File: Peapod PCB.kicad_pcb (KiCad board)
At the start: 2 copper layers, 16 parts, among them J1 CONN_01X01, J2 CONN_01X02, J3 CONN_01X06, J5 CONN_01X01, J6 CONN_01X01, J7 CONN_01X02, U1 ESP8266

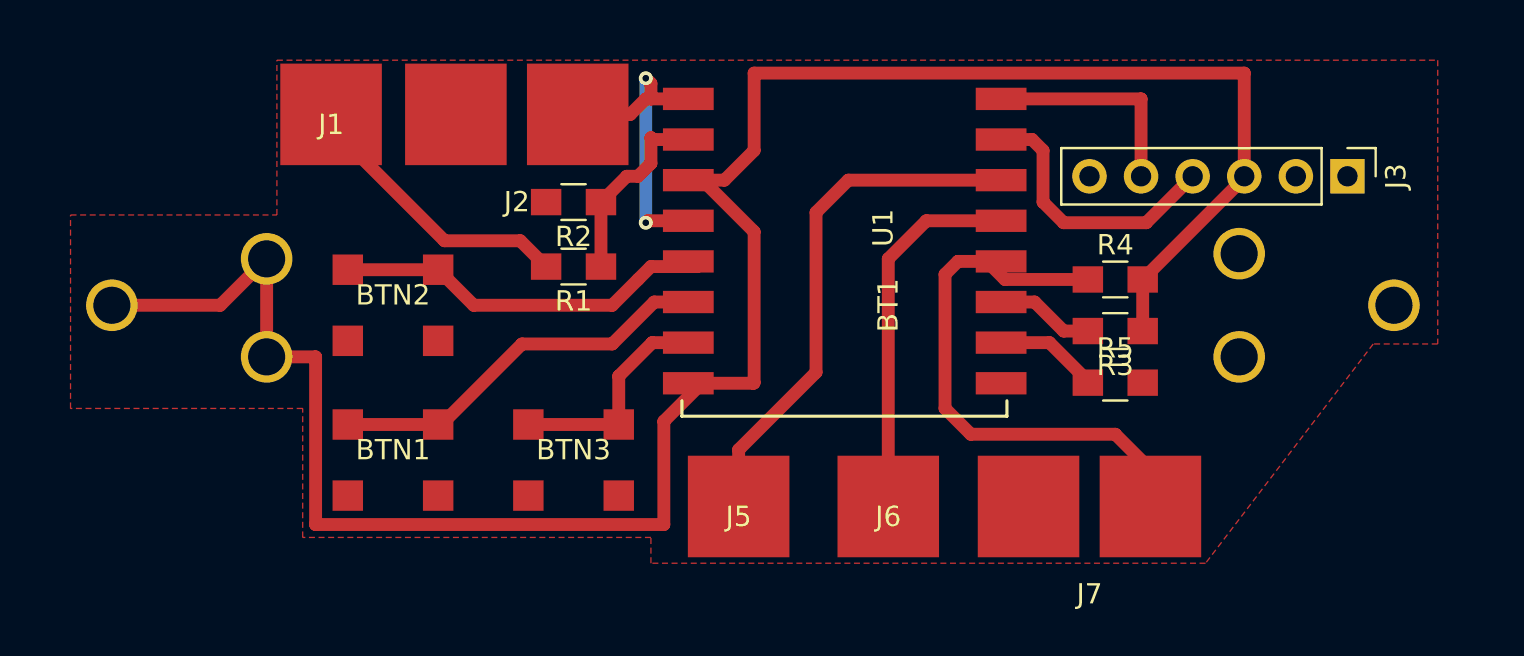
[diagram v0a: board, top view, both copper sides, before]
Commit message: changed copper to back plate
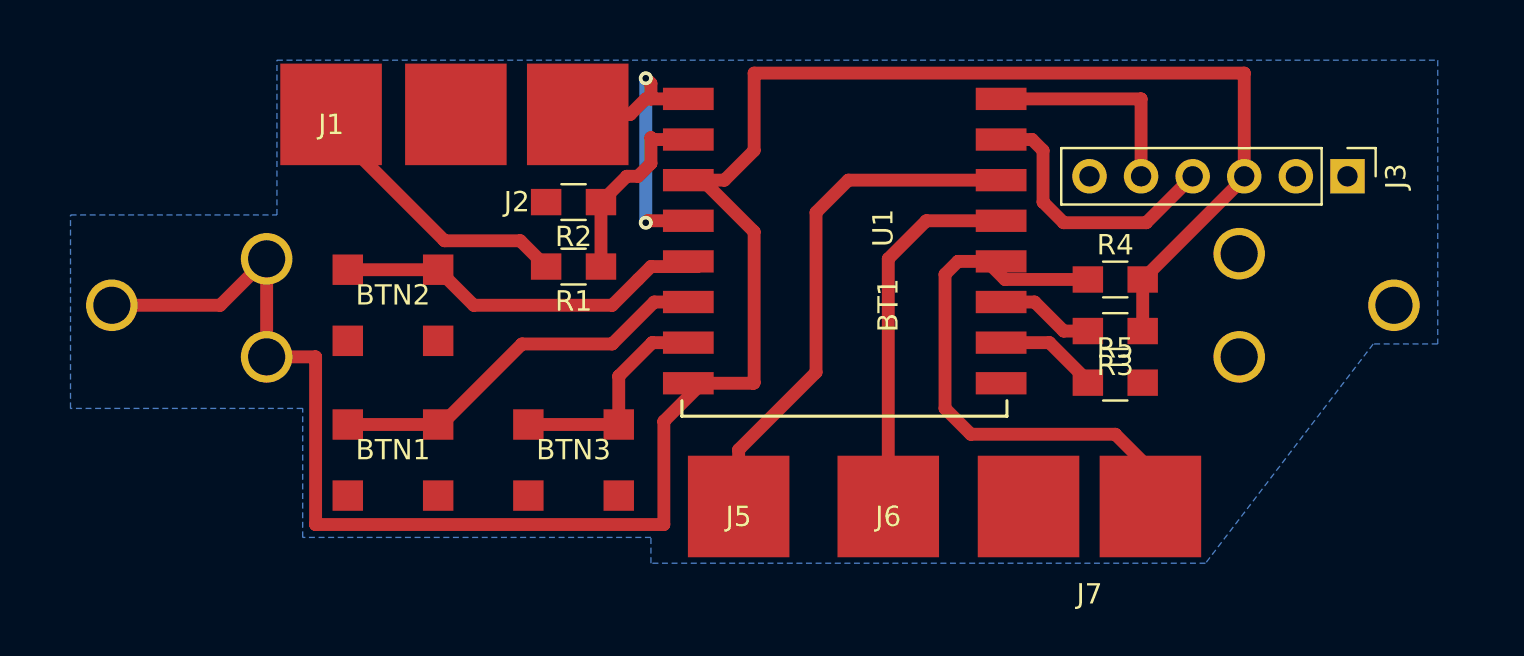
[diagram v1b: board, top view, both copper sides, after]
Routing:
- added copper zone on B.Cu, net GND
- removed copper zone on F.Cu, net GND
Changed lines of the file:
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@@
   (general
     (links 40)
-    (no_connects 4)
+    (no_connects 11)
     (area 154.305 20.282599 221.615001 54.6134)
     (thickness 1.6002)
@@
   (segment (start 204.39 43.1) (end 202.5 41.21) (width 0.635) (layer F.Cu) (net 17))
   (segment (start 202.5 41.21) (end 199.42 41.21) (width 0.635) (layer F.Cu) (net 17))
-  (zone (net 2) (net_name GND) (layer F.Cu) (hatch edge 0.508)
+  (zone (net 2) (net_name GND) (layer B.Cu) (hatch edge 0.508)
     (connect_pads (clearance 0.508))
     (min_thickness 0.254)

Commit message: stufff
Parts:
- added G***: LOGO, mod:LOGO, F.Cu at (159.5, 32.5)
- added J4: CONN_01X01, mod:Alligator Pad, F.Cu at (219.5, 49.3)
- added J8: CONN_01X01, mod:Alligator Pad, F.Cu at (213.4, 49.3)
- moved BTN2 12.7 mm to (160.0, 47.0)
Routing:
- net Net-(J3-Pad5): track 11.4 -> 47.3 mm, vias 0 -> 2
- net Net-(J3-Pad4): track 14.3 -> 30.8 mm, vias 0 -> 2
- net Net-(BTN2-Pad2): track 19.1 -> 32.4 mm
- net +3V3: track 108.4 -> 120.9 mm
- net GND: track 0.00 -> 0.20 mm, vias 0 -> 11
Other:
- board text added: "FSOSS 2017"

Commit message: Added labels
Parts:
- BRDG 2 RESET: renamed from J2
- VOTE :(: renamed from BTN3
- VOTE :): renamed from BTN2
- VOTE :|: renamed from BTN1
- moved ANALOG 1.27 mm to (165.9, 30.0)
- moved G*** 1.14 mm to (158.5, 33.0)
- renumbered J1 to ANALOG
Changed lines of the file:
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@@
     (34 B.Paste user)
     (35 F.Paste user)
-    (36 B.SilkS user)
+    (36 B.SilkS user hide)
     (37 F.SilkS user)
     (38 B.Mask user)
@@
   )
   (setup
-    (last_trace_width 0.635)
+    (last_trace_width 0.1524)
     (user_trace_width 0.381)
     (user_trace_width 0.635)
@@
   (module "mod:Bridge Pad" (layer F.Cu)
     (at 176.276 29.972)
-    (fp_text reference J2 (at 0 4.31) (layer F.SilkS)
-      (effects (font (size 1 1) (thickness 0.15)))
-    )
-    (fp_text value CONN_01X02 (at 0 3.31) (layer F.Fab)
+    (fp_text reference "BRDG 2 RESET" (at 0 2.032) (layer F.SilkS)
+      (effects (font (size 1 1) (thickness 0.15)))
+    )
+    (fp_text value CONN_01X02 (at 0 -1.524) (layer F.Fab)
       (effects (font (size 1 1) (thickness 0.15)))
     )
@@
   (module mod:Pushbutton (layer F.Cu)
     (at 170.18 46.99 180)
-    (fp_text reference BTN1 (at 0 0.5 180) (layer F.SilkS)
+    (fp_text reference "VOTE :|" (at 0 3.556 180) (layer F.SilkS)
       (effects (font (size 1 1) (thickness 0.15)))
     )
@@
   (module mod:Pushbutton (layer F.Cu)
     (at 160.02 46.99 180)
-    (fp_text reference BTN2 (at 0 0.5 180) (layer F.SilkS)
+    (fp_text reference "VOTE :)" (at 0 3.556 180) (layer F.SilkS)
       (effects (font (size 1 1) (thickness 0.15)))
     )
@@
   (module mod:Pushbutton (layer F.Cu)
     (at 179.07 46.99 180)
-    (fp_text reference BTN3 (at 0 0.5 180) (layer F.SilkS)
+    (fp_text reference "VOTE :(" (at 0 3.556 180) (layer F.SilkS)
       (effects (font (size 1 1) (thickness 0.15)))
     )
@@
   )
   (module "mod:Alligator Pad" (layer F.Cu)
-    (at 167.132 29.972)
-    (fp_text reference J1 (at 0 0.5) (layer F.SilkS)
-      (effects (font (size 1 1) (thickness 0.15)))
-    )
-    (fp_text value CONN_01X01 (at 0 -0.5) (layer F.Fab)
+    (at 165.862 29.972)
+    (fp_text reference ANALOG (at 0 3.302) (layer F.SilkS)
+      (effects (font (size 1 1) (thickness 0.15)))
+    )
+    (fp_text value CONN_01X01 (at 0 -1.524) (layer F.Fab)
       (effects (font (size 1 1) (thickness 0.15)))
     )
@@
   )
   (module mod:LOGO (layer F.Cu)
-    (at 159.512 32.512)
+    (at 158.496 33.02)
     (fp_text reference G*** (at 0 0) (layer F.SilkS) hide
       (effects (font (thickness 0.3)))

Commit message: Updated tracks
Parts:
- moved J6 1.02 mm to (194.6, 50.3)
- moved J5 0.76 mm to (187.2, 50.0)
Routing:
- net Net-(J6-Pad1): track 19.1 -> 21.4 mm
- net Net-(J1-Pad1): track 14.1 -> 15.0 mm
- net Net-(J5-Pad1): track 25.1 -> 25.9 mm
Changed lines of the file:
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@@
   )
   (module "mod:Alligator Pad" (layer F.Cu)
-    (at 187.198 49.276)
+    (at 187.198 50.038)
     (fp_text reference J5 (at 0 0.5) (layer F.SilkS)
       (effects (font (size 1 1) (thickness 0.15)))
@@
   )
   (module "mod:Alligator Pad" (layer F.Cu)
-    (at 194.564 49.276)
+    (at 194.564 50.292)
     (fp_text reference J6 (at 0 0.5) (layer F.SilkS)
       (effects (font (size 1 1) (thickness 0.15)))
@@
   (segment (start 181.295 42.86) (end 182.945 41.21) (width 0.635) (layer F.Cu) (net 5))
   (segment (start 181.13 45.24) (end 176.845 45.24) (width 0.635) (layer F.Cu) (net 5))
-  (segment (start 167.132 29.972) (end 167.132 30.607) (width 0.635) (layer F.Cu) (net 6))
-  (segment (start 167.132 30.607) (end 172.72 36.195) (width 0.635) (layer F.Cu) (net 6))
+  (segment (start 165.862 29.972) (end 165.862 30.607) (width 0.635) (layer F.Cu) (net 6))
+  (segment (start 165.862 30.607) (end 172.72 36.195) (width 0.635) (layer F.Cu) (net 6))
   (segment (start 172.72 36.195) (end 176.45 36.195) (width 0.635) (layer F.Cu) (net 6))
   (segment (start 176.45 36.195) (end 177.72 37.465) (width 0.635) (layer F.Cu) (net 6))
@@
   (segment (start 207.01 29.21) (end 207.01 29.972) (width 0.635) (layer F.Cu) (net 10))
   (segment (start 207.01 29.972) (end 207.01 33.02) (width 0.635) (layer F.Cu) (net 10))
-  (segment (start 187.198 49.276) (end 187.198 46.482) (width 0.635) (layer F.Cu) (net 12))
+  (segment (start 187.198 50.292) (end 187.198 47.498) (width 0.635) (layer F.Cu) (net 12))
   (segment (start 192.596 33.21) (end 199.42 33.21) (width 0.635) (layer F.Cu) (net 12))
   (segment (start 191.008 34.798) (end 192.596 33.21) (width 0.635) (layer F.Cu) (net 12))
   (segment (start 191.008 42.672) (end 191.008 34.798) (width 0.635) (layer F.Cu) (net 12))
-  (segment (start 187.198 46.482) (end 191.008 42.672) (width 0.635) (layer F.Cu) (net 12))
-  (segment (start 194.564 49.276) (end 194.564 37.084) (width 0.635) (layer F.Cu) (net 13))
+  (segment (start 187.198 47.498) (end 191.008 42.672) (width 0.635) (layer F.Cu) (net 12))
+  (segment (start 194.564 50.546) (end 194.564 38.354) (width 0.635) (layer F.Cu) (net 13))
   (segment (start 196.438 35.21) (end 199.42 35.21) (width 0.635) (layer F.Cu) (net 13))
-  (segment (start 194.564 37.084) (end 196.438 35.21) (width 0.635) (layer F.Cu) (net 13))
-  (segment (start 194.564 49.276) (end 194.564 48.006) (width 0.635) (layer F.Cu) (net 13) (status 30))
+  (segment (start 194.564 38.354) (end 196.438 35.21) (width 0.635) (layer F.Cu) (net 13))
+  (segment (start 194.564 50.546) (end 194.564 48.006) (width 0.635) (layer F.Cu) (net 13) (status 30))
   (segment (start 207.47 49.276) (end 207.47 47.45) (width 0.635) (layer F.Cu) (net 14))
   (segment (start 207.47 47.45) (end 205.74 45.72) (width 0.635) (layer F.Cu) (net 14))

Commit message: final??
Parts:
- added G***: LOGO, mod:fsoss, B.Cu at (159.3, 47.2)
- FTDI 3.3V: renamed from J3
- moved TX 1.05 mm to (219.7, 50.3)
- moved GPIO0 1.05 mm to (204.2, 50.3)
- moved RX 1.02 mm to (213.4, 50.3)
- moved BRDG 2 RESET 0.72 mm to (175.8, 29.5)
- moved ANALOG 0.57 mm to (166.1, 29.5)
- moved GPIO5 0.25 mm to (187.2, 50.3)
- renumbered J7 to GPIO0, J6 to GPIO4, J5 to GPIO5, J8 to RX, J4 to TX
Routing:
- net GND: track 0.20 -> 23.6 mm, vias 11 -> 6
- net Net-(J6-Pad1): track 21.4 -> 18.8 mm
- net Net-(J7-Pad1): track 27.4 -> 28.3 mm
- net Net-(J3-Pad5): track 47.3 -> 48.1 mm
- net Net-(J3-Pad4): track 30.8 -> 31.5 mm
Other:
- board outline added: 70.9 x 26.9 mm
- board text added: "GND"

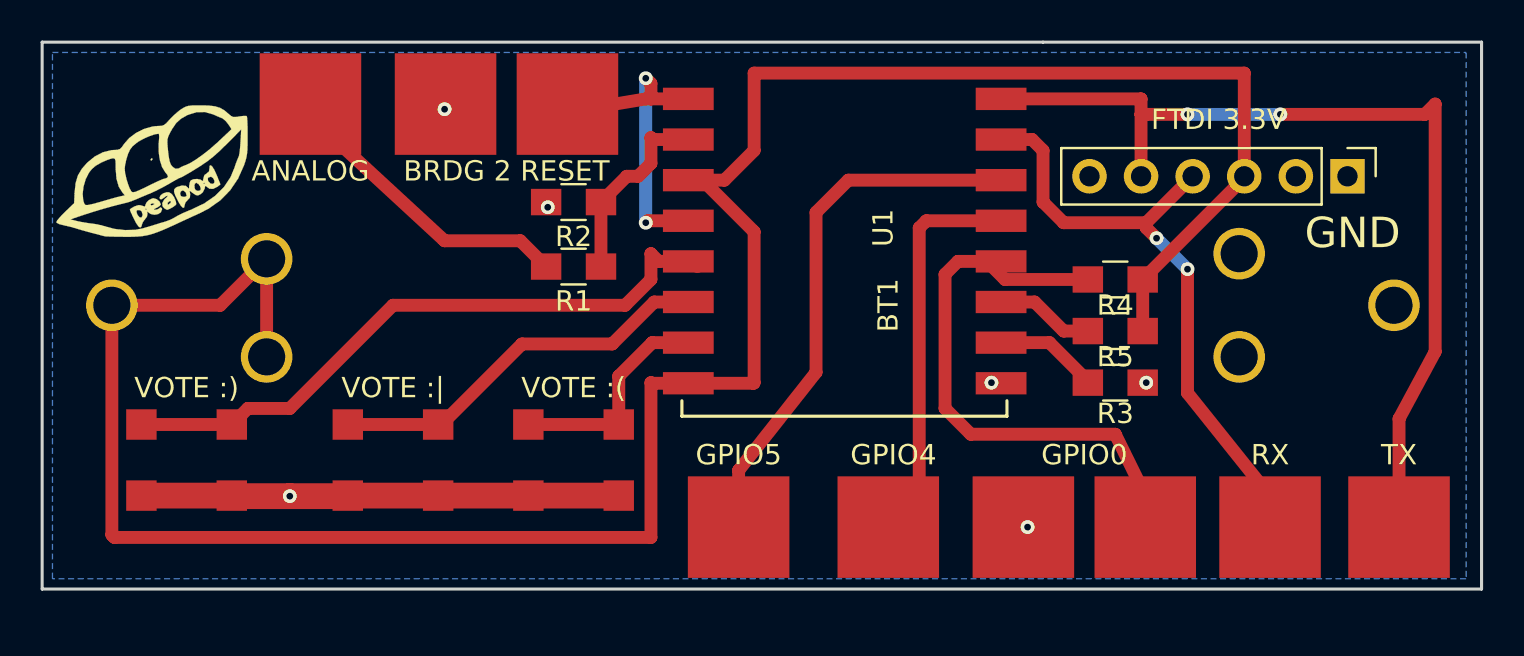
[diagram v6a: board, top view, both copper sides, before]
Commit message: Made wire routes nicer
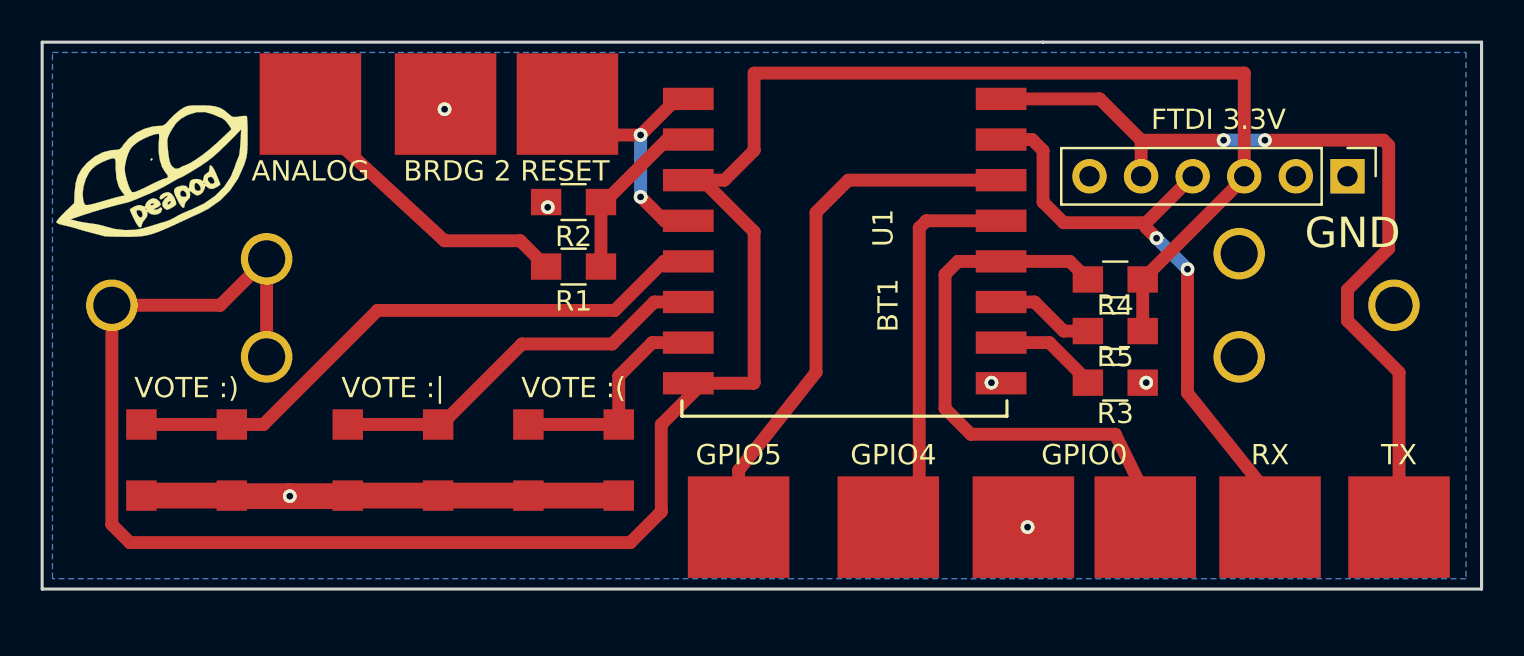
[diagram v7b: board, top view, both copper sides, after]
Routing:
- net Net-(J3-Pad5): track 48.1 -> 43.2 mm
- net Net-(J2-Pad1): track 19.3 -> 14.6 mm
- net +3V3: track 120.9 -> 118.9 mm
- net Net-(BTN2-Pad2): track 32.4 -> 31.0 mm
- net Net-(R1-Pad1): track 10.3 -> 9.45 mm
